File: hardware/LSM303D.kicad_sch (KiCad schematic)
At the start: 11 parts, among them J1 SDA, J2 SCL, J3 GND, J4 3.3V, U1 LSM303D

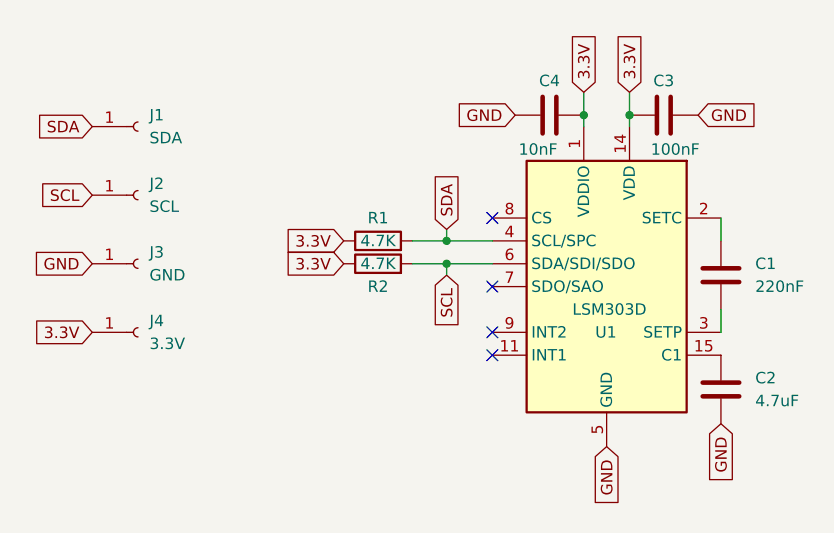
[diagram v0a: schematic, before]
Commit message: fix footprint
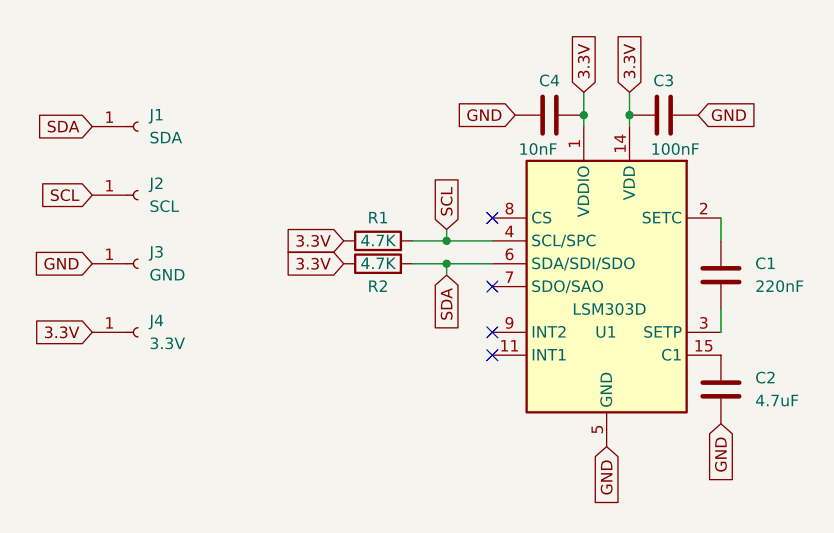
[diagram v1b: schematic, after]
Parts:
- U1: footprint Package_LGA:LGA-16_3x3mm_P0.5mm -> Package_LGA:LGA-16_3x3mm_P0.5mm_LayoutBorder3x5y
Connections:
- net SCL: now also R1.2, U1.4 (SCL/SPC); no longer R2.2, U1.6 (SDA/SDI/SDO)
- net SDA: now also R2.2, U1.6 (SDA/SDI/SDO); no longer R1.2, U1.4 (SCL/SPC)
